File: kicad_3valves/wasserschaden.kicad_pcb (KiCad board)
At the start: 2 copper layers, 50 x 50 mm, 30 parts, among them J1 v1 out, J2 12V in, J3 sense, J4 v2 out, J5 v3 out, U1 stepdown, U2 WeMos_mini, U3 DS18B20

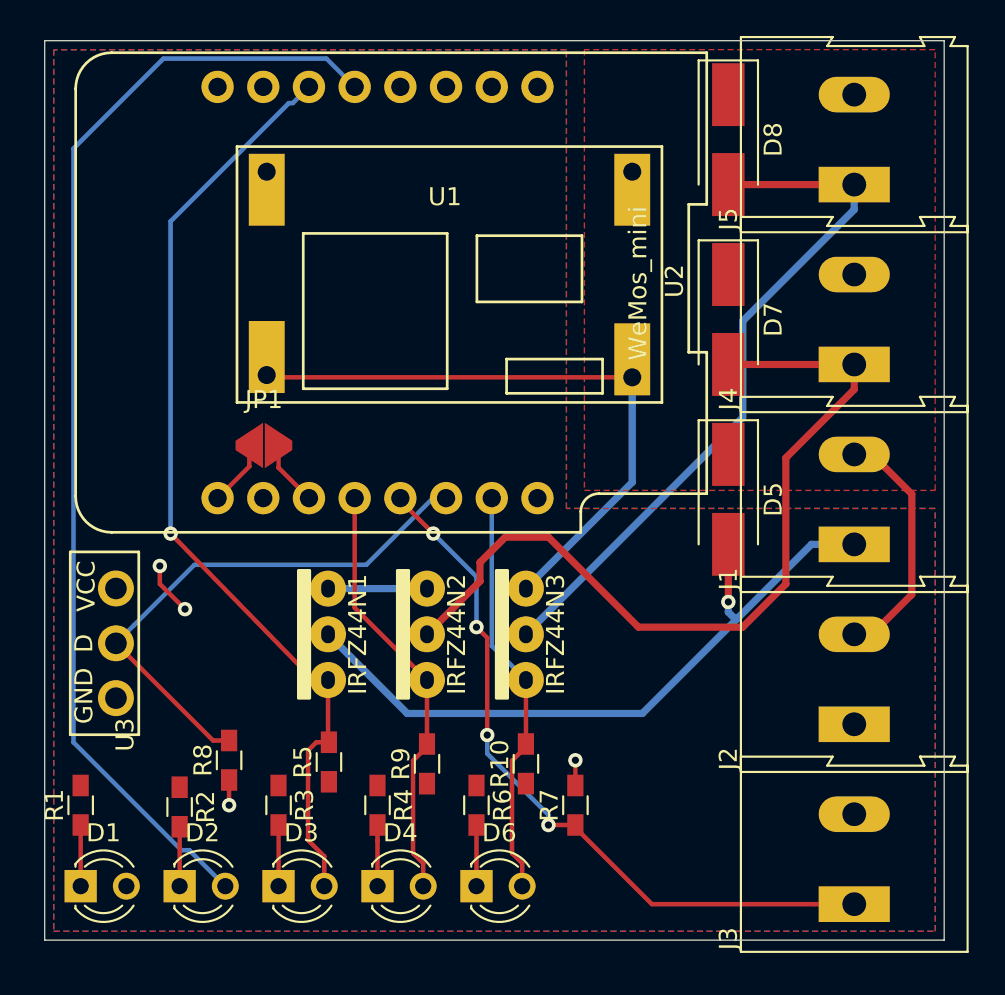
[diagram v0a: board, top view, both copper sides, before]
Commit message: fancy routing for 3 valve board
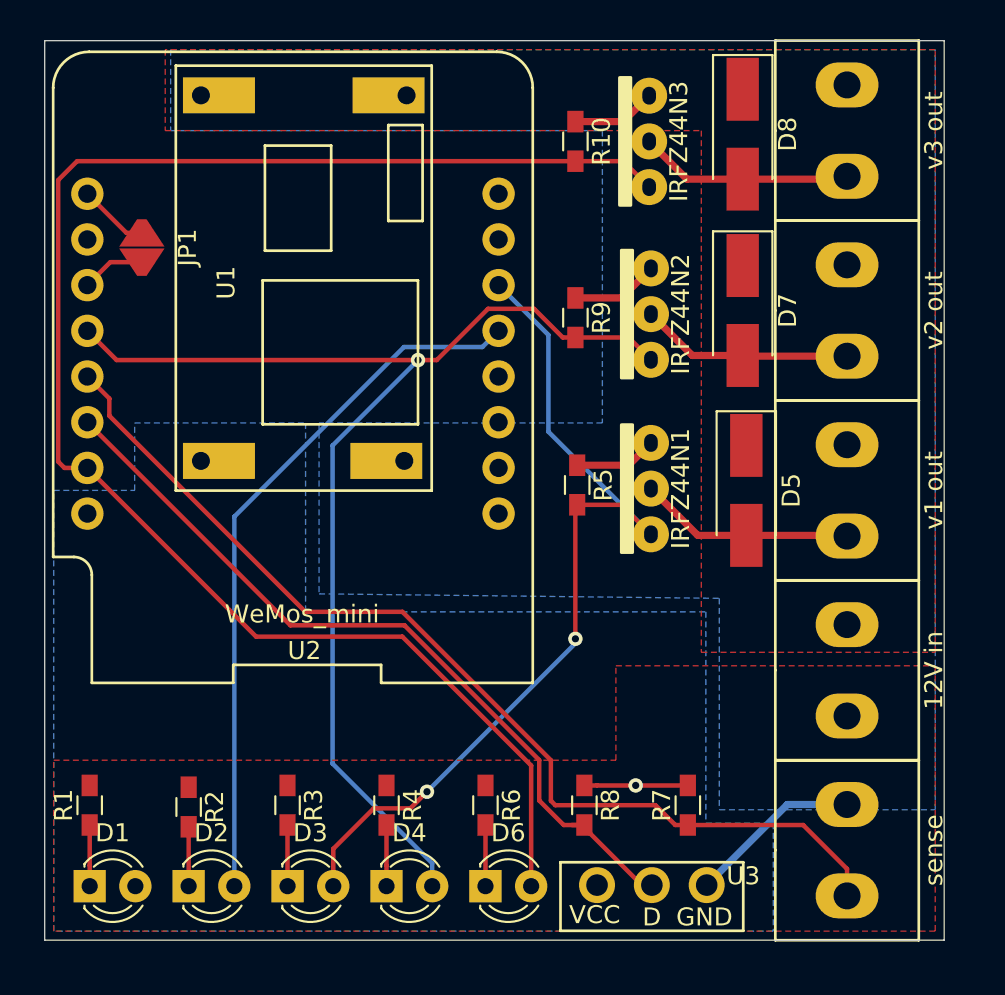
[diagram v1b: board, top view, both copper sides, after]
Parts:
- J1, J2, J3, J4, J5: footprint Connectors_Terminal_Blocks:TerminalBlock_Altech_AK300-2_P5.00mm -> custom:termina_2pin
- moved R10 34.7 mm to (94.5, 65.6), turned to 270 degrees
- moved U3 29.3 mm to (98.8, 104.4), turned to 180 degrees
- moved IRFZ44N3 28.2 mm to (98.6, 65.6)
- moved R9 26.1 mm to (94.5, 75.4), turned to 270 degrees
- moved IRFZ44N2 21.7 mm to (98.7, 75.2)
- moved R5 20.7 mm to (94.6, 84.7), turned to 270 degrees
- moved R8 19.9 mm to (95.0, 102.5), turned to 270 degrees
- moved IRFZ44N1 19.7 mm to (98.7, 84.9)
- moved JP1 12.9 mm to (70.4, 71.5), turned to 90 degrees
- moved U1 8.10 mm to (79.4, 73.2), turned to 270 degrees
- moved R7 6.25 mm to (100.8, 102.5)
- moved U2 5.80 mm to (78.8, 77.4), turned to 90 degrees
- moved J1 3.03 mm to (109.6, 85.0)
- moved J2 3.03 mm to (109.6, 95.0)
- moved J3 3.03 mm to (109.6, 105.0)
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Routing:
- net v3: track 22.7 -> 89.5 mm
- net v2: track 23.6 -> 68.0 mm, vias 0 -> 1
- net Net-(D7-Pad2): track 46.6 -> 11.9 mm
- net Net-(D8-Pad2): track 39.6 -> 11.9 mm
- net Net-(D5-Pad2): track 39.4 -> 12.0 mm, vias 1 -> 0
- net info: track 63.1 -> 39.5 mm
- net sense: track 40.5 -> 56.9 mm, vias 4 -> 0
- net GND: track 40.1 -> 23.8 mm
- net temp: track 30.2 -> 44.1 mm
- net +12V: track 13.8 -> 0.00 mm
- net v1: track 53.1 -> 50.1 mm, vias 1 -> 2
- net +3V3: track 5.78 -> 5.75 mm, vias 4 -> 1
- added copper zone on B.Cu, net GND
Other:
- net class jp added: clearance 0, trace_width 0.25, via_dia 0.8, via_drill 0.4

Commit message: 3 valve pcb
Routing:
- net v3: track 89.5 -> 80.6 mm
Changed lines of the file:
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@@
     (thickness 1.6)
     (drawings 4)
-    (tracks 103)
+    (tracks 102)
     (zones 0)
     (modules 30)
@@
   (segment (start 104 87.5) (end 109.56 87.5) (width 0.4) (layer F.Cu) (net 10))
   (segment (start 89.5 107) (end 89.5 103.6) (width 0.25) (layer F.Cu) (net 11))
-  (segment (start 66.097208 83.75) (end 65.75 83.402792) (width 0.25) (layer F.Cu) (net 12))
-  (segment (start 67.37 83.75) (end 66.097208 83.75) (width 0.25) (layer F.Cu) (net 12))
-  (segment (start 65.75 83.402792) (end 65.75 67.75) (width 0.25) (layer F.Cu) (net 12))
-  (segment (start 66.8 66.7) (end 94.5 66.7) (width 0.25) (layer F.Cu) (net 12))
-  (segment (start 65.75 67.75) (end 66.8 66.7) (width 0.25) (layer F.Cu) (net 12))
   (segment (start 76.75 93.13) (end 84.88 93.13) (width 0.25) (layer F.Cu) (net 12))
   (segment (start 67.37 83.75) (end 76.75 93.13) (width 0.25) (layer F.Cu) (net 12))
@@
   (segment (start 97.16 66.7) (end 98.6 68.14) (width 0.25) (layer F.Cu) (net 12))
   (segment (start 94.5 66.7) (end 97.16 66.7) (width 0.25) (layer F.Cu) (net 12))
+  (segment (start 97.600001 69.139999) (end 98.6 68.14) (width 0.25) (layer B.Cu) (net 12))
+  (segment (start 97.004999 69.735001) (end 97.600001 69.139999) (width 0.25) (layer B.Cu) (net 12))
+  (segment (start 81.384999 69.735001) (end 97.004999 69.735001) (width 0.25) (layer B.Cu) (net 12))
+  (segment (start 67.37 83.75) (end 81.384999 69.735001) (width 0.25) (layer B.Cu) (net 12))
   (segment (start 101 77.5) (end 103.8 77.5) (width 0.4) (layer F.Cu) (net 13))
   (segment (start 98.7 75.2) (end 101 77.5) (width 0.4) (layer F.Cu) (net 13))
